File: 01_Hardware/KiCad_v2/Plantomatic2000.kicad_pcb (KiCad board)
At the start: 4 copper layers, 46.7 x 21.4 mm, 295 parts, among them J100 TYPE-C-31-M-12, J300 JST_B2B, J600 JST_B2B, J601 JST_B2B, J700 JST_B4B, J701 JST_B4B, J800 Conn_02x03_Odd_Even, J801 JST_B2B, J802 JST_B2B, J803 JST_B2B, J804 Conn_02x05_Odd_Even, J805 JST_B2B, J806 JST_B2B, J807 JST_B2B, J808 JST_B2B, Q100 UMH3N, Q113 CSD17313Q2, Q200 SI7615DN-T1-GE3, Q201 SI7615DN-T1-GE3, Q202 DMP6050SSD-13, Q203 IRLML2402TRPBF, Q204 SI7615DN-T1-GE3, Q205 IRLML2402TRPBF, Q300 BSS314PEH6327, Q301 IRLML2402TRPBF, Q500 IRLML2402TRPBF, Q600 STN3NF06L, Q601 STN3NF06L, Q700 BSS314PEH6327, Q701 BSS314PEH6327, Q702 IRLML2402TRPBF, Q703 IRLML2402TRPBF, SW800 SW_Push, SW801 SW_Push, U100 USBLC6-2P6, U101 CP2102N-A02-GQFN24R, U104 TPS61287RZPR, U200 CYPD3177-24LQ, U300 BQ25892, U403 XC6220B331MR-G, U404 XC6220B331MR-G, U405 LM1085IS-12/NOPB, U406 LM1085IS-12/NOPB, U500 DS3231M, U501 ESP32-WROOM-32E-N4, U502 AT24CS01-SSHM

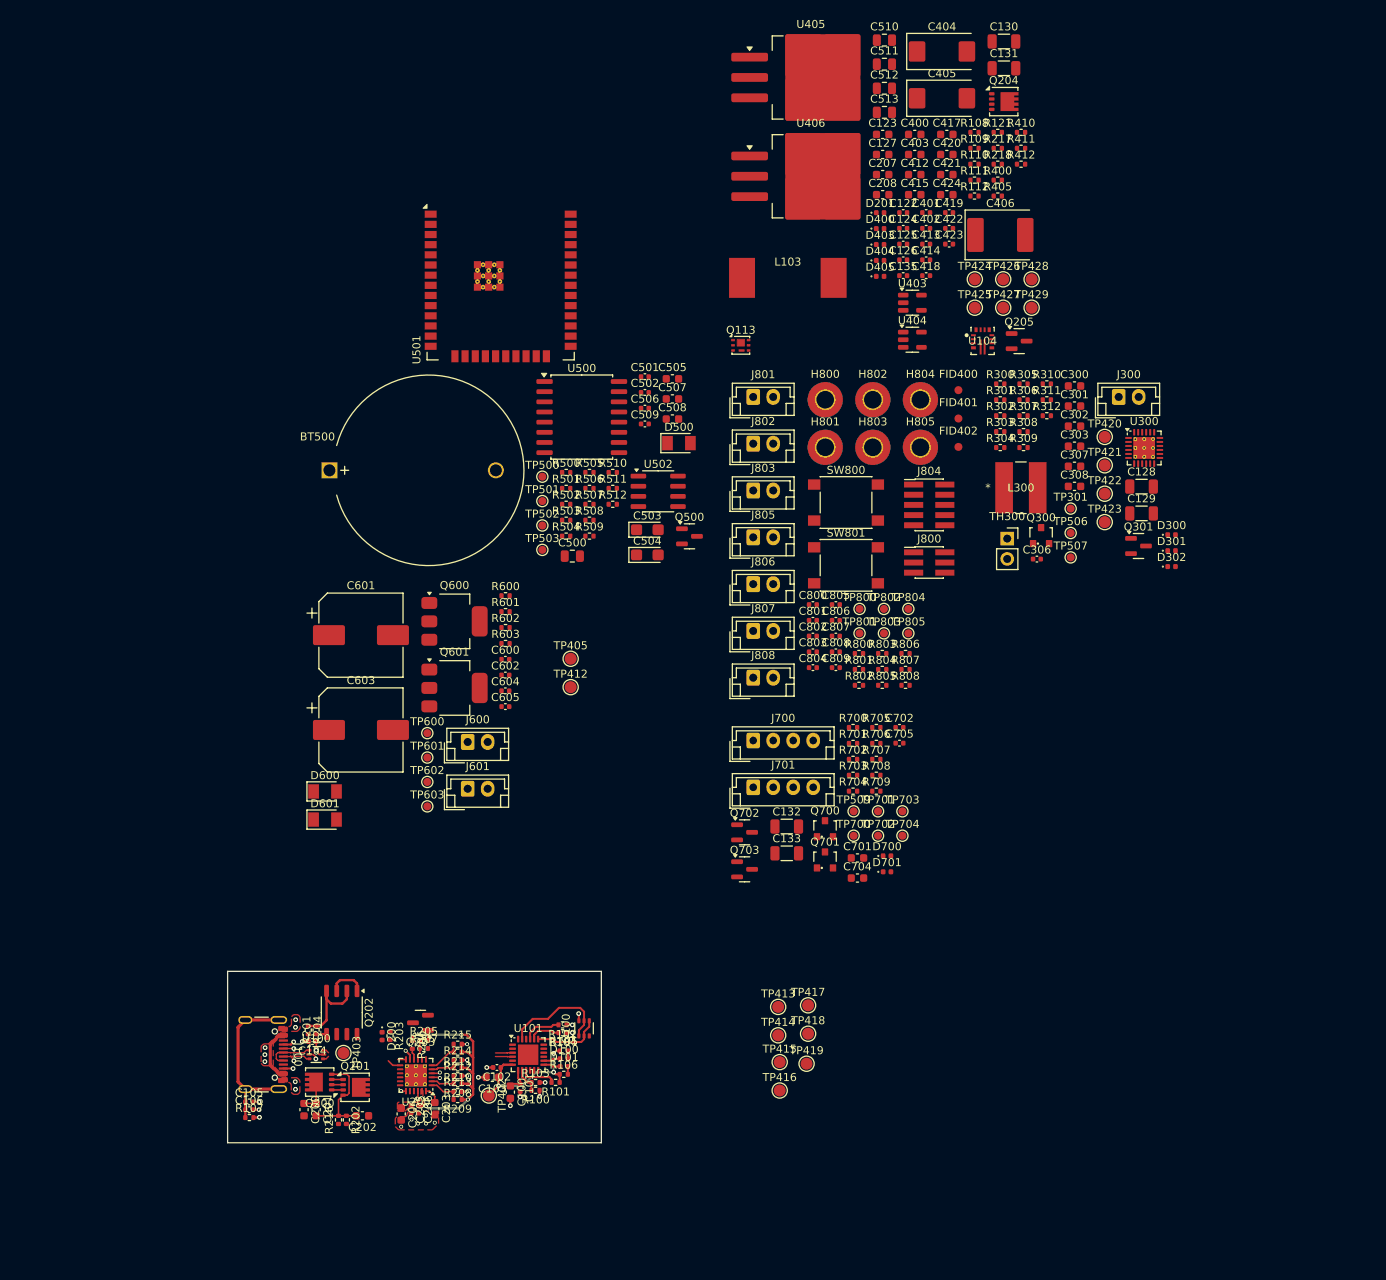
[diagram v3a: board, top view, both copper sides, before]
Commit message: Power plane/rearranged connectors
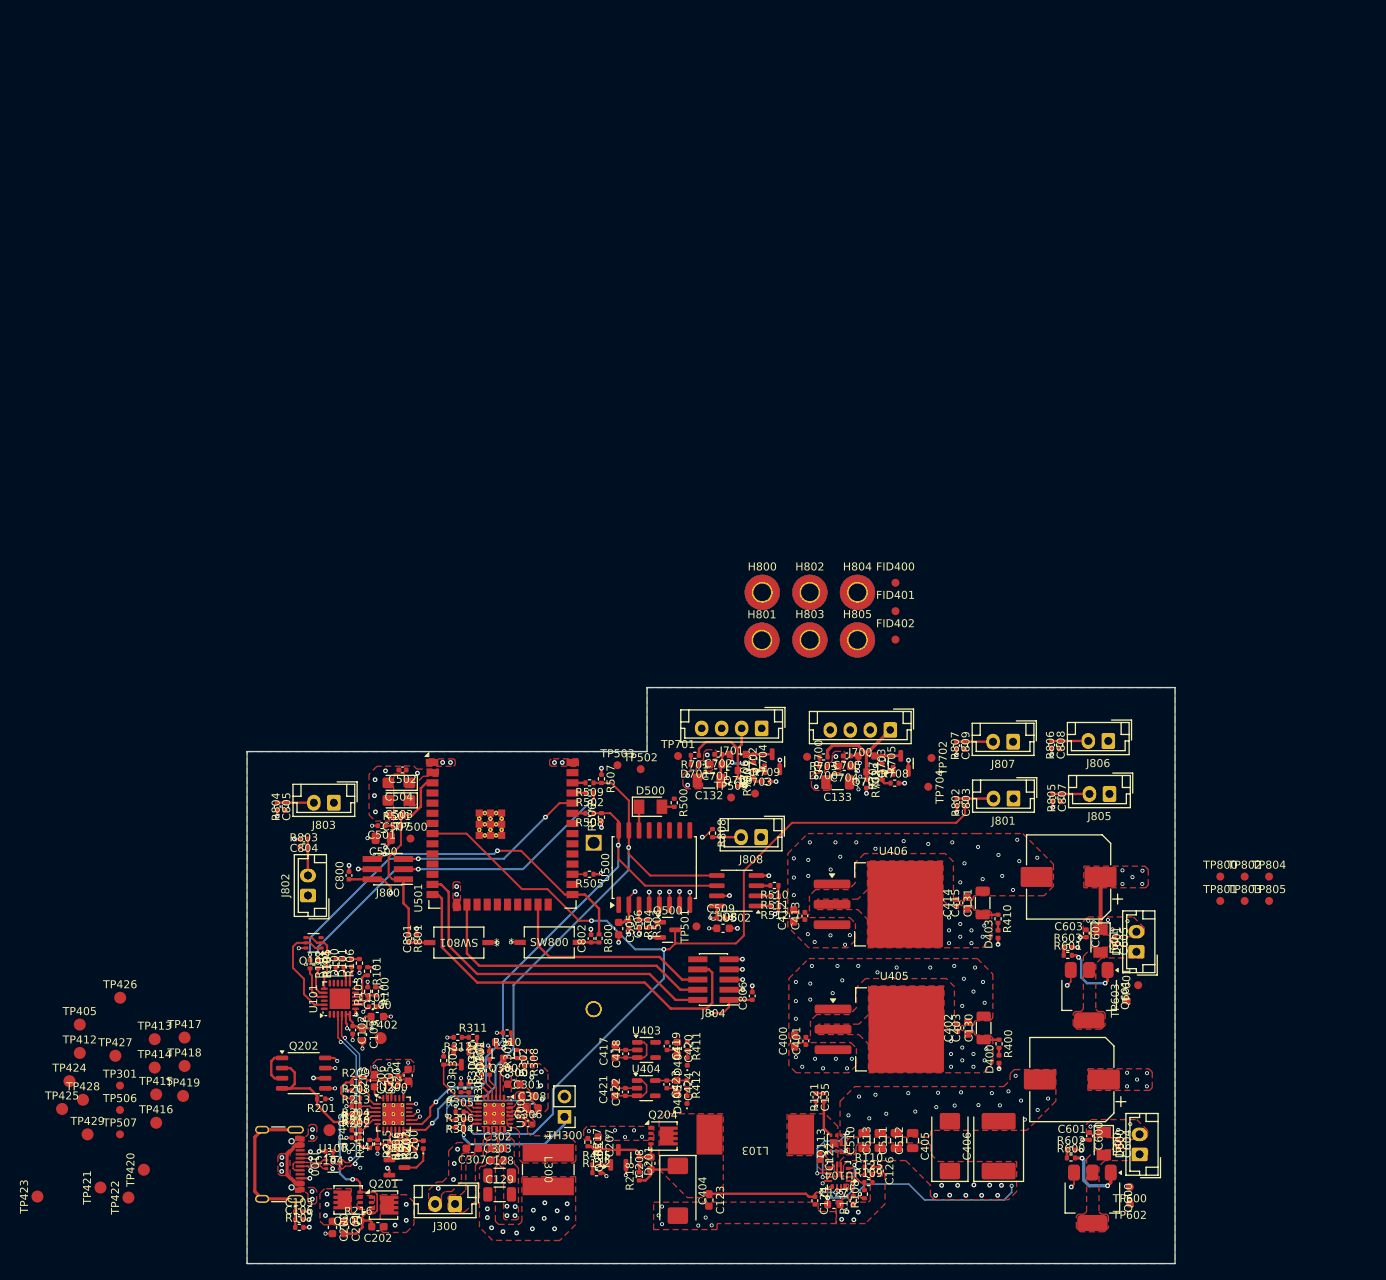
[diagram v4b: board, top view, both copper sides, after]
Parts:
- BT500: moved to B.Cu
- SW800, SW801: footprint Button_Switch_SMD:SW_SPST_PTS645 -> Custom_Global_Footprints:SW_101-C-W_XKB
- TH300: footprint Connector_PinSocket_2.54mm:PinSocket_1x02_P2.54mm_Vertical -> Connector_PinHeader_2.54mm:PinHeader_1x02_P2.54mm_Vertical
- moved TP423 157.8 mm to (85.4, 169.5), turned to 90 degrees
- moved TP429 156.9 mm to (91.7, 161.8)
- moved TP428 156.8 mm to (91.1, 157.4)
- moved TP421 154.6 mm to (93.3, 168.4), turned to 90 degrees
- moved TP425 151.8 mm to (88.5, 158.6)
- moved TP424 151.2 mm to (89.4, 155.1)
- moved TP420 151.1 mm to (98.7, 166.2), turned to 90 degrees
- moved TP422 150.4 mm to (96.8, 169.7), turned to 90 degrees
- moved C404 146.2 mm to (165.4, 168.8), turned to -90 degrees
- moved TP427 145.1 mm to (95.1, 151.9)
- moved TP426 142.3 mm to (95.7, 144.7)
- moved TP301 139.0 mm to (95.7, 155.7)
- moved TP506 139.0 mm to (95.7, 158.7)
- moved TP507 139.0 mm to (95.7, 161.8)
- moved C510 137.6 mm to (188.7, 162.5), turned to 90 degrees
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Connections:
- net /DC_DC_REGULATORS/SW renamed /DC_DC_REGULATORS/BOOT_SW
- net Net-(C306-Pad1) renamed /BATTERY_MANAGEMENT_IC/SW
- net Net-(D600-A) renamed /PUMPS/PUMP_1_DRAIN
- net Net-(D601-A) renamed /PUMPS/PUMP_2_DRAIN
- net Net-(Q113-G) renamed /DC_DC_REGULATORS/BOOST_DRV
- net Net-(Q200-S-Pad1) renamed /USB_C_POWER_DELIVERY/Drain
- net Net-(Q204-D) renamed /DC_DC_REGULATORS/BOOST_VIN
- net Net-(U104-BOOT) renamed /DC_DC_REGULATORS/BOOT
- net Net-(U104-COMP) renamed /DC_DC_REGULATORS/BOOST_COMP
- net Net-(U104-FB) renamed /DC_DC_REGULATORS/BOOST_FB
- net Net-(U104-ILIM) renamed /DC_DC_REGULATORS/BOOST_ILIM
- net Net-(U104-MODE) renamed /DC_DC_REGULATORS/B_VCC
- net Net-(U300-BTST) renamed /BATTERY_MANAGEMENT_IC/BTST
- net Net-(U300-PMID) renamed /BATTERY_MANAGEMENT_IC/PMID
- C400 pad 1: +13V -> +12V
- C401 pad 1: +13V -> +12V
- C412 pad 1: +13V -> +12V
- C413 pad 1: +13V -> +12V
- C500 pad 1: +3V3 -> +3V3_MCU
- C501 pad 1: +3V3 -> +3V3_MCU
- C502 pad 1: +3V3 -> +3V3_MCU
- C503 pad 1: +3V3 -> +3V3_MCU
- C504 pad 1: +3V3 -> +3V3_MCU
- C505 pad 1: +3V3 -> +3V3_MCU
- C506 pad 1: +3V3 -> +3V3_MCU
- C508 pad 1: +3V3 -> +3V3_MCU
- C509 pad 1: +3V3 -> +3V3_MCU
- R202 pad 1: /USB_C_POWER_DELIVERY/VBUS_FET_EN -> Net-(U200-VBUS_FET_EN)
- R202 pad 2: Net-(U200-VBUS_FET_EN) -> /USB_C_POWER_DELIVERY/VBUS_FET_EN
- R500 pad 1: +3V3 -> +3V3_MCU
- R501 pad 1: +3V3 -> +3V3_MCU
- R505 pad 1: Net-(U501-IO16) -> +3V3_MCU
- R505 pad 2: +3V3 -> Net-(U501-IO16)
- R506 pad 1: +3V3 -> +3V3_MCU
- R507 pad 1: +3V3 -> +3V3_MCU
- R510 pad 1: +3V3 -> +3V3_MCU
- R511 pad 1: +3V3 -> +3V3_MCU
- R512 pad 1: +3V3 -> +3V3_MCU
- U405 pad 3: +13V -> +12V
- U406 pad 3: +13V -> +12V
- U500 pad 2: +3V3 -> +3V3_MCU
- U501 pad 2: +3V3 -> +3V3_MCU
- U502 pad 8: +3V3 -> +3V3_MCU
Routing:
- net WAKE_SLEEP: track 0.00 -> 126.8 mm, vias 0 -> 3
- net GND: track 12.6 -> 93.7 mm, vias 26 -> 188
- net ESP_SDA: track 1.03 -> 76.2 mm, vias 0 -> 3
- net ESP_SCL: track 1.72 -> 72.7 mm, vias 0 -> 3
- net ESP_TDI: track 0.00 -> 50.5 mm
- net ESP_TX: track 0.71 -> 46.4 mm, vias 1 -> 3
- net ESP_RX: track 0.71 -> 44.4 mm, vias 1 -> 3
- net ESP_TMS: track 0.00 -> 43.1 mm
- net ESP_TCK: track 0.00 -> 36.9 mm
- net ESP_IO0: track 0.91 -> 35.9 mm, vias 1 -> 3
- net ESP_TDO: track 0.00 -> 26.9 mm
- net /DC_DC_REGULATORS/BOOST_VIN: track 0.00 -> 24.7 mm, vias 0 -> 3
- net ESP_EN: track 0.00 -> 24.2 mm
- net +12V: track 0.00 -> 22.9 mm, vias 0 -> 24
- net /USB_C_TO_SERIAL/USB_D-: track 2.96 -> 22.1 mm, vias 0 -> 2
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- added copper zone on F.Cu, net +12V
- added copper zone on In2.Cu, net +12V
- added copper zone on F.Cu, net +12V_PUMP
- added copper zone on In2.Cu, net +12V_PUMP
- added copper zone on F.Cu, net +12V_WATER
- added copper zone on In2.Cu, net +12V_WATER
- added copper zone on In2.Cu, net +3V3
- added copper zone on F.Cu, net +3V3_MCU
- added copper zone on In2.Cu, net +3V3_MCU
- added copper zone on F.Cu, net +5V
- added copper zone on In2.Cu, net +5V
- added copper zone on F.Cu, net +VBAT
- added copper zone on In2.Cu, net +VBUS
- added copper zone on In2.Cu, net +VDD
- added copper zone on F.Cu, net +VSYS
- added copper zone on In2.Cu, net +VSYS
- added copper zone on F.Cu, net /BATTERY_MANAGEMENT_IC/BTST
- added copper zone on F.Cu, net /BATTERY_MANAGEMENT_IC/REGN
- added copper zone on F.Cu, net /BATTERY_MANAGEMENT_IC/SW
- added copper zone on F.Cu, net /DC_DC_REGULATORS/BOOST_DRV
- added copper zone on F.Cu, net /DC_DC_REGULATORS/BOOST_VIN
- added copper zone on F.Cu, net /DC_DC_REGULATORS/BOOT
- added copper zone on F.Cu, net /DC_DC_REGULATORS/BOOT_SW
- added copper zone on F.Cu, net /PUMPS/PUMP_1_DRAIN
- added copper zone on F.Cu, net /PUMPS/PUMP_2_DRAIN
- added copper zone on F.Cu, net /USB_C_POWER_DELIVERY/Drain
- added copper zone on B.Cu, net GND
- added copper zone on In1.Cu, net GND
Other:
- board size 46.7 x 21.4 mm -> 116 x 72 mm

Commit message: Hardware for manufacturing v0.2
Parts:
- removed the G*** at (401.6, 225.9)
- removed TP415, TP416, TP417, TP418, TP421, TP425: TestPoint_Small, TestPoint:TestPoint_Pad_D1.5mm
- added +VBAT: TestPoint_Small, TestPoint:TestPoint_Pad_D1.0mm, F.Cu at (126.9, 138.6)
- added C407: 4.7nF, Capacitor_SMD:C_0402_1005Metric, F.Cu at (211.2, 115.6)
- added C408: 4.7nF, Capacitor_SMD:C_0402_1005Metric, F.Cu at (161.4, 139.0)
- added C409: 4.7nF, Capacitor_SMD:C_0402_1005Metric, F.Cu at (103.2, 113.7)
- added C410: 4.7nF, Capacitor_SMD:C_0402_1005Metric, F.Cu at (102.3, 96.6)
- added C411: 4.7nF, Capacitor_SMD:C_0402_1005Metric, F.Cu at (167.8, 76.3)
- added C416: 4.7nF, Capacitor_SMD:C_0402_1005Metric, B.Cu at (211.1, 109.4)
- added C425: 4.7nF, Capacitor_SMD:C_0402_1005Metric, B.Cu at (191.5, 138.9)
- added C426: 4.7nF, Capacitor_SMD:C_0402_1005Metric, B.Cu at (126.7, 138.9)
- added C427: 4.7nF, Capacitor_SMD:C_0402_1005Metric, B.Cu at (103.1, 91.4)
- added C428: 4.7nF, Capacitor_SMD:C_0402_1005Metric, B.Cu at (153.6, 76.5)
- added F400: Polyfuse_Small, Fuse:Fuse_1210_3225Metric, F.Cu at (119.2, 139.2)
- added F401: Polyfuse_Small, Fuse:Fuse_1210_3225Metric, F.Cu at (111.7, 117.8)
- added G***: LOGO, LOGO, F.Cu at (131.2, 108.0)
- added G***: LOGO, LOGO, B.Cu at (162.3, 129.2)
- added GND: TestPoint, TestPoint:TestPoint_Pad_1.5x1.5mm, F.Cu at (197.0, 107.7)
- added GND: TestPoint, TestPoint:TestPoint_Pad_1.5x1.5mm, F.Cu at (163.7, 101.4)
- added GND: TestPoint, TestPoint:TestPoint_Pad_1.5x1.5mm, F.Cu at (164.3, 112.6)
- added GND: TestPoint, TestPoint:TestPoint_Pad_1.5x1.5mm, F.Cu at (181.7, 137.6)
- added GND: TestPoint, TestPoint:TestPoint_Pad_1.5x1.5mm, F.Cu at (122.6, 109.2)
- added R401: 22R, Resistor_SMD:R_0402_1005Metric, F.Cu at (211.7, 113.9)
- added R402: 511K, Resistor_SMD:R_0402_1005Metric, F.Cu at (211.8, 83.9)
- added R403: 511K, Resistor_SMD:R_0402_1005Metric, F.Cu at (168.6, 139.7)
- added R404: 511K, Resistor_SMD:R_0402_1005Metric, F.Cu at (102.4, 103.9)
- added R406: 511K, Resistor_SMD:R_0402_1005Metric, B.Cu at (157.1, 139.5)
- added R407: 22R, Resistor_SMD:R_0402_1005Metric, F.Cu at (163.1, 139.5)
- added R408: 22R, Resistor_SMD:R_0402_1005Metric, F.Cu at (102.7, 115.3)
- added R409: 22R, Resistor_SMD:R_0402_1005Metric, F.Cu at (102.3, 94.4)
- added R413: 22R, Resistor_SMD:R_0402_1005Metric, F.Cu at (167.8, 74.3)
- added R414: 22R, Resistor_SMD:R_0402_1005Metric, B.Cu at (211.6, 107.9)
- added R415: 22R, Resistor_SMD:R_0402_1005Metric, B.Cu at (193.1, 139.4)
- added R416: 22R, Resistor_SMD:R_0402_1005Metric, B.Cu at (128.2, 139.4)
- added R417: 22R, Resistor_SMD:R_0402_1005Metric, B.Cu at (102.6, 89.9)
- added R418: 22R, Resistor_SMD:R_0402_1005Metric, B.Cu at (153.6, 74.5)
- added R419: 511K, Resistor_SMD:R_0402_1005Metric, B.Cu at (202.1, 74.3)
- added R420: 511K, Resistor_SMD:R_0402_1005Metric, B.Cu at (126.1, 82.3)
- +12V: renamed from TP424; footprint TestPoint:TestPoint_Pad_D1.5mm -> TestPoint:TestPoint_Pad_D1.0mm
- +12V_P: renamed from TP426; footprint TestPoint:TestPoint_Pad_D1.5mm -> TestPoint:TestPoint_Pad_D1.0mm
- +12V_W: renamed from TP427; footprint TestPoint:TestPoint_Pad_D1.5mm -> TestPoint:TestPoint_Pad_D1.0mm
- +3V3: renamed from TP429; footprint TestPoint:TestPoint_Pad_D1.5mm -> TestPoint:TestPoint_Pad_D1.0mm
- +3V3_MCU: renamed from TP428; footprint TestPoint:TestPoint_Pad_D1.5mm -> TestPoint:TestPoint_Pad_D1.0mm
- +VBUS: renamed from TP403; footprint TestPoint:TestPoint_Pad_D1.5mm -> TestPoint:TestPoint_Pad_D1.0mm
- +VDD: renamed from TP402; footprint TestPoint:TestPoint_Pad_D1.5mm -> TestPoint:TestPoint_Pad_D1.0mm
- +VDDD: renamed from TP413; footprint TestPoint:TestPoint_Pad_D1.5mm -> TestPoint:TestPoint_Pad_D1.0mm
- +VSYS: renamed from TP423; footprint TestPoint:TestPoint_Pad_D1.5mm -> TestPoint:TestPoint_Pad_D1.0mm
- DTR: renamed from TP405; footprint TestPoint:TestPoint_Pad_D1.5mm -> TestPoint:TestPoint_Pad_D1.0mm
- EN: renamed from TP419; footprint TestPoint:TestPoint_Pad_D1.5mm -> TestPoint:TestPoint_Pad_D1.0mm
- OTG: renamed from TP420; footprint TestPoint:TestPoint_Pad_D1.5mm -> TestPoint:TestPoint_Pad_D1.0mm
- RTS: renamed from TP412; footprint TestPoint:TestPoint_Pad_D1.5mm -> TestPoint:TestPoint_Pad_D1.0mm
- SEN: renamed from TP414; footprint TestPoint:TestPoint_Pad_D1.5mm -> TestPoint:TestPoint_Pad_D1.0mm
- SLEEP: renamed from TP422; footprint TestPoint:TestPoint_Pad_D1.5mm -> TestPoint:TestPoint_Pad_D1.0mm
- moved START 135.3 mm to (107.5, 88.3)
- moved LINE_SEL 128.6 mm to (110.5, 94.4)
- moved +12V_W 109.5 mm to (194.1, 104.9)
- moved +12V_P 104.4 mm to (195.1, 112.8)
- moved +12V 84.1 mm to (164.4, 117.1)
- moved FID400 82.7 mm to (110.0, 88.9)
- moved SLEEP 79.8 mm to (162.9, 91.8)
- moved +3V3 77.1 mm to (156.2, 119.5)
- moved H801 72.5 mm to (104.0, 109.0)
- moved +3V3_MCU 70.7 mm to (112.3, 90.0)
- moved RESET 70.0 mm to (192.3, 80.7)
- moved +VSYS 66.2 mm to (142.2, 135.4)
- moved MIN 62.8 mm to (192.4, 87.7)
- moved PSEL 62.8 mm to (137.1, 114.5)
- moved HOUR 60.2 mm to (204.2, 80.7)
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- renumbered TP509 to +3V3_DISP, TP700 to +3V3_WP, TP506 to CE, TP301 to CE_EN, TP703 to DEN, TP701 to DENP, TP500 to EN, TP804 to HOUR, TP801 to LINE_SEL, TP803 to MIN, TP600 to P1D, TP602 to P1EN, TP601 to P2D, TP603 to P2EN, TP507 to PSEL, TP805 to RESET, TP501 to RSLEEP, TP502 to SCL, TP503 to SDA, TP800 to SLEEP, TP802 to START, TP704 to WEN, TP702 to WENP
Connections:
- net /DISPLAY_AND_WATER_ENABLE/WATER_SENSOR_EN renamed /MICROCONTROLLER/WATER_EN
- net Net-(J100-SHIELD) renamed /USB_C_TO_SERIAL/shield
- C202 pad 1: +5V -> /USB_C_POWER_DELIVERY/fuse_5A
- Q201 pad 5: +5V -> /USB_C_POWER_DELIVERY/fuse_5A
- Q202 pad 7: +5V -> /USB_C_POWER_DELIVERY/Fuse_1A
- Q202 pad 8: +5V -> /USB_C_POWER_DELIVERY/Fuse_1A
- R112 pad 1: /DC_DC_REGULATORS/BOOST_ENABLE -> /MICROCONTROLLER/BOOST_EN
- R311 pad 1: /BATTERY_MANAGEMENT_IC/CHARGE_ENABLE -> /MICROCONTROLLER/CHARGE_EN
- R312 pad 1: /BATTERY_MANAGEMENT_IC/CHARGE_ENABLE -> /MICROCONTROLLER/CHARGE_EN
- R405 pad 1: /DC_DC_REGULATORS/BOOST_ENABLE -> /MICROCONTROLLER/BOOST_EN
- R803 pad 1: /CONNECTORS/SELECT_LINE_BUTTON_PIN -> /MICROCONTROLLER/SELECT_LINE_PIN
- R804 pad 1: ESP_TMS -> /MICROCONTROLLER/START_PIN
- R805 pad 1: /CONNECTORS/MIN_BUTTON_PIN -> /MICROCONTROLLER/MIN_PIN
- R806 pad 1: /CONNECTORS/HOUR_BUTTON_PIN -> /MICROCONTROLLER/HOUR_PIN
- R807 pad 1: /CONNECTORS/RESET_BUTTON_PIN -> /MICROCONTROLLER/RESET_PIN
- U200 pad 11: +5V -> /USB_C_POWER_DELIVERY/fuse_5A
- U501 pad 10: /CONNECTORS/SELECT_LINE_BUTTON_PIN -> /MICROCONTROLLER/CHARGE_EN
- U501 pad 11: /CONNECTORS/MIN_BUTTON_PIN -> /MICROCONTROLLER/PUMP2_EN
- U501 pad 12: /CONNECTORS/HOUR_BUTTON_PIN -> /MICROCONTROLLER/PUMP1_EN
- U501 pad 24: /MICROCONTROLLER/DISP_EN -> /MICROCONTROLLER/BOOST_EN
- U501 pad 26: /MICROCONTROLLER/WATER_SIG -> WAKE_SLEEP
- U501 pad 28: /BATTERY_MANAGEMENT_IC/CHARGE_ENABLE -> /MICROCONTROLLER/MIN_PIN
- U501 pad 29: unconnected-(U501-IO5-Pad29) -> /MICROCONTROLLER/HOUR_PIN
- U501 pad 30: /MICROCONTROLLER/PUMP2_EN -> /MICROCONTROLLER/RESET_PIN
- U501 pad 31: /MICROCONTROLLER/PUMP1_EN -> /MICROCONTROLLER/WATER_SIG
- U501 pad 6: /DC_DC_REGULATORS/BOOST_ENABLE -> /MICROCONTROLLER/START_PIN
- U501 pad 7: unconnected-(U501-IO35-Pad7) -> /MICROCONTROLLER/SELECT_LINE_PIN
- U501 pad 8: WAKE_SLEEP -> /MICROCONTROLLER/DISP_EN
- U501 pad 9: /CONNECTORS/RESET_BUTTON_PIN -> unconnected-(U501-IO33-Pad9)
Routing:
- net /MICROCONTROLLER/PUMP1_EN: track 1.00 -> 108.1 mm, vias 0 -> 2
- net /MICROCONTROLLER/PUMP2_EN: track 1.00 -> 90.3 mm, vias 0 -> 2
- net /MICROCONTROLLER/HOUR_PIN: track 0.00 -> 67.2 mm, vias 0 -> 2
- net /MICROCONTROLLER/RESET_PIN: track 0.00 -> 57.0 mm, vias 0 -> 2
- net /MICROCONTROLLER/MIN_PIN: track 0.00 -> 52.7 mm, vias 0 -> 2
- net /MICROCONTROLLER/DISP_EN: track 1.38 -> 47.6 mm, vias 0 -> 2
- net +3V3: track 14.1 -> 59.3 mm, vias 3 -> 8
- net /MICROCONTROLLER/WATER_EN: track 1.33 -> 45.5 mm, vias 0 -> 2
- net /MICROCONTROLLER/WATER_SIG: track 0.00 -> 43.1 mm, vias 0 -> 1
- net /USB_C_TO_SERIAL/shield: track 21.3 -> 59.8 mm, vias 0 -> 168
- net /BATTERY_MANAGEMENT_IC/VBUS_FET_SAFE_EN: track 17.4 -> 54.0 mm
- net /MICROCONTROLLER/BOOST_EN: track 0.00 -> 36.2 mm, vias 0 -> 2
- net WAKE_SLEEP: track 126.8 -> 92.9 mm, vias 3 -> 2
- net GND: track 93.7 -> 124.1 mm, vias 188 -> 312
- net /MICROCONTROLLER/CHARGE_EN: track 0.00 -> 27.3 mm, vias 0 -> 2
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- added copper zone on F.Cu, net +3V3
- added copper zone on In2.Cu, net +VDDD
- added copper zone on F.Cu, net /BATTERY_MANAGEMENT_IC/PMID
- added copper zone on F.Cu, net /USB_C_POWER_DELIVERY/Fuse_1A
- added copper zone on F.Cu, net /USB_C_POWER_DELIVERY/fuse_5A
- added copper zone on B.Cu, net /USB_C_TO_SERIAL/shield
- added copper zone on F.Cu, net /USB_C_TO_SERIAL/shield
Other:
- outline, holes or cut-outs redrawn
- board text added: "+3V3"
- board text added: "+VBAT"
- board text added: "BOOT"
- board text added: "CR2032"
- board text added: "GND"
- board text added: "GND GND GND GND +VBUS"
- board text added: "IO2: BOOST_ENABLE IO4: WAKE_SLEEP IO5: HOURS IO17: MINUTES IO18: EXTERNAL_RESET IO19: WATER_SIGNAL IO23: WATER_SENSOR_ENABLE IO25: BATTERY CHARGE ENABLE IO26: PUMP_2_ENABLE IO27: PUMP_1_ENABLE IO32: DISPLAY_ENABLE IO34: START_BUTTON IO35: SELECT_LINE"
- board text added: "N/C TDI TDO TCK TMS"
- board text added: "ON LED"
- board text added: "Plantomatic v0.2 20251116"
- board text added: "RESET"
- board text added: "SCL"
- board text added: "SDA"
- board text added: "SIG"
- board text removed: "Plantomatic2000 v0.1 20250625"
